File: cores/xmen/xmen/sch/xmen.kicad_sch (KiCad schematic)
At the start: 12 parts, among them CN1 Conn_02x32_Row_Letter_First, CN6 Conn_01x15, CN7 Conn_01x15

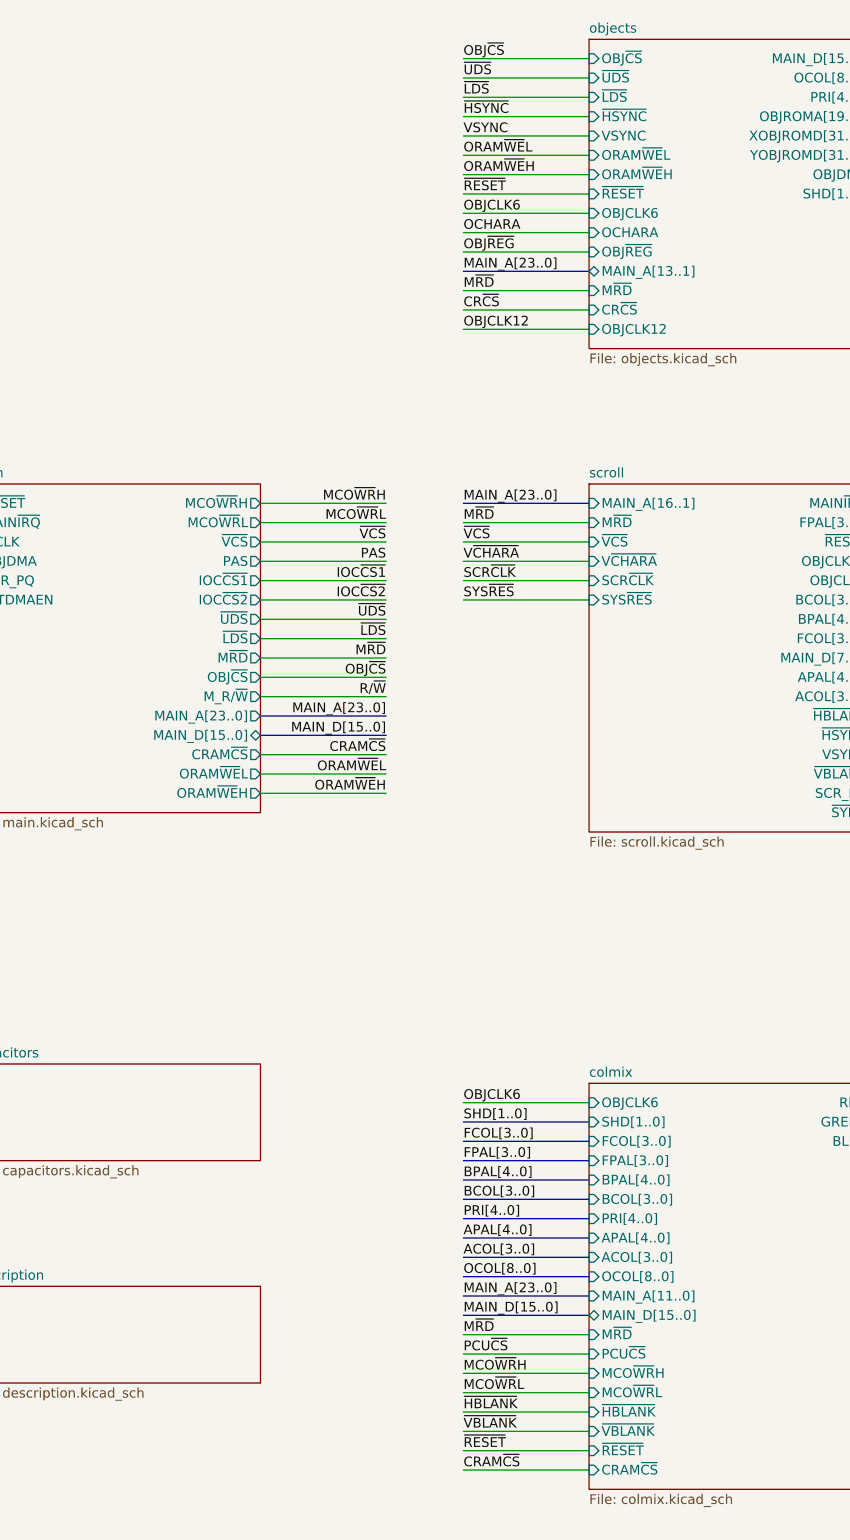
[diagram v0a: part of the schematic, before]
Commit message: Modification of signal names and pin order symbol 053246. Correction of MB8464
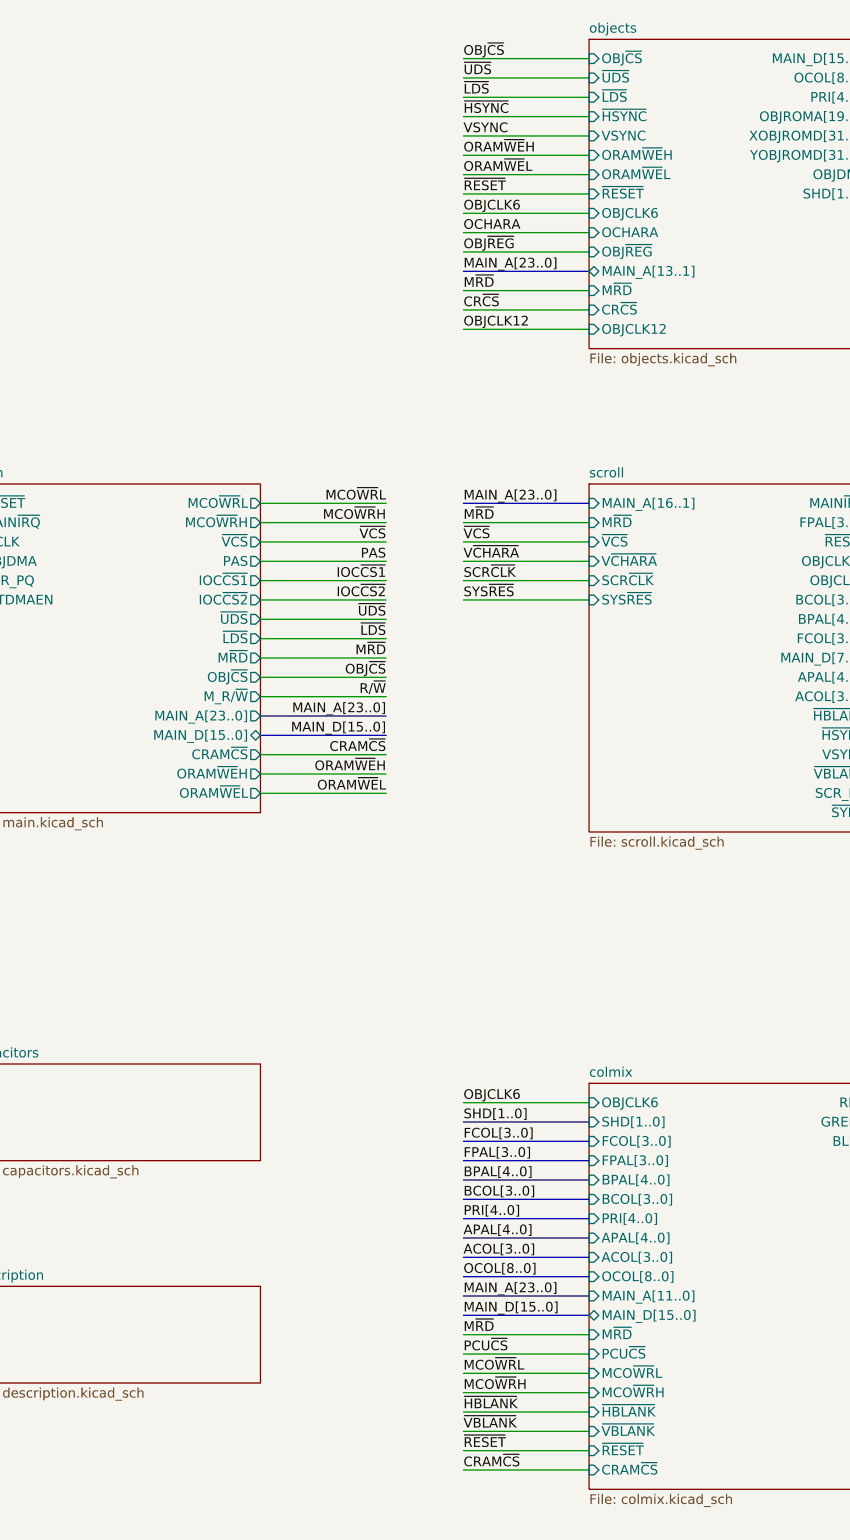
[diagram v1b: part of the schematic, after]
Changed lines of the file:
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@@
     (effects (font (size 1.27 1.27)) (justify right bottom))
   )
-  (label "MCO~{WR}H" (at 313.69 205.74 0) (fields_autoplaced)
+  (label "MCO~{WR}L" (at 313.69 205.74 0) (fields_autoplaced)
     (effects (font (size 1.27 1.27)) (justify left bottom))
   )
@@
     (effects (font (size 1.27 1.27)) (justify right bottom))
   )
-  (label "MCO~{WR}H" (at 303.53 91.44 180) (fields_autoplaced)
+  (label "MCO~{WR}L" (at 303.53 91.44 180) (fields_autoplaced)
     (effects (font (size 1.27 1.27)) (justify right bottom))
   )
@@
     (effects (font (size 1.27 1.27)) (justify right bottom))
   )
-  (label "MCO~{WR}L" (at 303.53 93.98 180) (fields_autoplaced)
+  (label "MCO~{WR}H" (at 303.53 93.98 180) (fields_autoplaced)
     (effects (font (size 1.27 1.27)) (justify right bottom))
   )
@@
     (effects (font (size 1.27 1.27)) (justify left bottom))
   )
-  (label "MCO~{WR}L" (at 313.69 208.28 0) (fields_autoplaced)
+  (label "MCO~{WR}H" (at 313.69 208.28 0) (fields_autoplaced)
     (effects (font (size 1.27 1.27)) (justify left bottom))
   )
@@
     (effects (font (size 1.27 1.27)) (justify left bottom))
   )
-  (label "ORAM~{WE}H" (at 313.69 48.26 0) (fields_autoplaced)
+  (label "ORAM~{WE}L" (at 313.69 48.26 0) (fields_autoplaced)
     (effects (font (size 1.27 1.27)) (justify left bottom))
   )
@@
     (effects (font (size 1.27 1.27)) (justify right bottom))
   )
-  (label "ORAM~{WE}L" (at 313.69 45.72 0) (fields_autoplaced)
+  (label "ORAM~{WE}H" (at 313.69 45.72 0) (fields_autoplaced)
     (effects (font (size 1.27 1.27)) (justify left bottom))
   )
@@
     (effects (font (size 1.27 1.27)) (justify left bottom))
   )
-  (label "ORAM~{WE}L" (at 303.53 127 180) (fields_autoplaced)
+  (label "ORAM~{WE}H" (at 303.53 127 180) (fields_autoplaced)
     (effects (font (size 1.27 1.27)) (justify right bottom))
   )
@@
     (effects (font (size 1.27 1.27)) (justify right bottom))
   )
-  (label "ORAM~{WE}H" (at 303.53 129.54 180) (fields_autoplaced)
+  (label "ORAM~{WE}L" (at 303.53 129.54 180) (fields_autoplaced)
     (effects (font (size 1.27 1.27)) (justify right bottom))
   )
@@
       (effects (font (size 1.27 1.27)) (justify right))
     )
-    (pin "ORAM~{WE}L" output (at 287.02 127 0)
-      (effects (font (size 1.27 1.27)) (justify right))
-    )
-    (pin "ORAM~{WE}H" output (at 287.02 129.54 0)
+    (pin "ORAM~{WE}H" output (at 287.02 127 0)
+      (effects (font (size 1.27 1.27)) (justify right))
+    )
+    (pin "ORAM~{WE}L" output (at 287.02 129.54 0)
       (effects (font (size 1.27 1.27)) (justify right))
     )
@@
       (effects (font (size 1.27 1.27)) (justify right))
     )
-    (pin "MCO~{WR}L" output (at 287.02 93.98 0)
-      (effects (font (size 1.27 1.27)) (justify right))
-    )
-    (pin "MCO~{WR}H" output (at 287.02 91.44 0)
+    (pin "MCO~{WR}H" output (at 287.02 93.98 0)
+      (effects (font (size 1.27 1.27)) (justify right))
+    )
+    (pin "MCO~{WR}L" output (at 287.02 91.44 0)
       (effects (font (size 1.27 1.27)) (justify right))
     )
@@
       (effects (font (size 1.27 1.27)) (justify left top))
     )
-    (pin "ORAM~{WE}L" input (at 330.2 45.72 180)
-      (effects (font (size 1.27 1.27)) (justify left))
-    )
-    (pin "ORAM~{WE}H" input (at 330.2 48.26 180)
+    (pin "ORAM~{WE}H" input (at 330.2 45.72 180)
+      (effects (font (size 1.27 1.27)) (justify left))
+    )
+    (pin "ORAM~{WE}L" input (at 330.2 48.26 180)
       (effects (font (size 1.27 1.27)) (justify left))
     )
@@
       (effects (font (size 1.27 1.27)) (justify left))
     )
-    (pin "MCO~{WR}H" input (at 330.2 205.74 180)
-      (effects (font (size 1.27 1.27)) (justify left))
-    )
-    (pin "MCO~{WR}L" input (at 330.2 208.28 180)
-      (effects (font (size 1.27 1.27)) (justify left))
-    )
+    (pin "MCO~{WR}L" input (at 330.2 205.74 180)
+      (effects (font (size 1.27 1.27)) (justify left))
+    )
+    (pin "MCO~{WR}H" input (at 330.2 208.28 180)
+      (effects (font (size 1.27 1.27)) (justify left))
+    )
